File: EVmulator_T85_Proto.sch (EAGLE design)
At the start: 24 parts, among them Q2 DMN3404L-7, U1 ATTINY85V

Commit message: Finished compact version
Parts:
- added J2: (no value), Eigene-Rietig:TAG-CONNECT_TC2030-MCP-NL
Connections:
- new net !RESET: J2.5
- new net MISO: J2.1
- new net MOSI: J2.4
- new net SCK: J2.3
- new net VCC: J2.2
- net GND: now also J2.6
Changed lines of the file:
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@@
 <part name="R10" library="rcl" library_urn="urn:adsk.eagle:library:334" deviceset="R-EU_" device="R0603" package3d_urn="urn:adsk.eagle:package:23555/3" value="1k"/>
 <part name="Q2" library="SparkFun-DiscreteSemi" library_urn="urn:adsk.eagle:library:514" deviceset="MOSFET-NCH" device="-AO3404A" package3d_urn="urn:adsk.eagle:package:38446/1" value="DMN3404L-7"/>
+<part name="J2" library="Eigene-Rietig" library_urn="urn:adsk.eagle:library:40964436" deviceset="TAG-CONNECT_TC2030" device="-MCP-NL" package3d_urn="urn:adsk.eagle:package:41146494/1"/>
+<part name="GND12" library="supply1" library_urn="urn:adsk.eagle:library:371" deviceset="GND" device=""/>
 </parts>
 <sheets>
@@
 <text x="220.98" y="55.88" size="1.778" layer="91">6pin TagConnect
 Pinout 6pin ISP compatible</text>
+<text x="195.58" y="50.8" size="1.27" layer="91">ISP</text>
+<text x="170.18" y="55.88" size="1.778" layer="91">6pin TagConnect
+Pinout 6pin ISP compatible</text>
 </plain>
 <instances>
@@
 <attribute name="NAME" x="198.12" y="129.54" size="1.778" layer="96" rot="R180"/>
 <attribute name="VALUE" x="198.12" y="106.68" size="1.778" layer="96" rot="R90"/>
+</instance>
+<instance part="J2" gate="G$1" x="190.5" y="53.34" smashed="yes"/>
+<instance part="GND12" gate="1" x="185.42" y="33.02" smashed="yes">
+<attribute name="VALUE" x="182.88" y="30.48" size="1.778" layer="96"/>
 </instance>
 </instances>
@@
 <pinref part="R9" gate="G$1" pin="1"/>
 <wire x1="177.8" y1="86.36" x2="177.8" y2="88.9" width="0.1524" layer="91"/>
+</segment>
+<segment>
+<pinref part="J2" gate="G$1" pin="6"/>
+<pinref part="GND12" gate="1" pin="GND"/>
+<wire x1="187.96" y1="38.1" x2="185.42" y2="38.1" width="0.1524" layer="91"/>
+<wire x1="185.42" y1="38.1" x2="185.42" y2="35.56" width="0.1524" layer="91"/>
 </segment>
 </net>
@@
 </segment>
 </net>
+<net name="MOSI" class="0">
+<segment>
+<wire x1="182.88" y1="43.18" x2="187.96" y2="43.18" width="0.1524" layer="91"/>
+<pinref part="J2" gate="G$1" pin="4"/>
+<label x="182.88" y="43.18" size="1.27" layer="95" rot="R180" xref="yes"/>
+</segment>
+</net>
+<net name="!RESET" class="0">
+<segment>
+<wire x1="182.88" y1="40.64" x2="187.96" y2="40.64" width="0.1524" layer="91"/>
+<pinref part="J2" gate="G$1" pin="5"/>
+<label x="182.88" y="40.64" size="1.27" layer="95" rot="R180" xref="yes"/>
+</segment>
+</net>
+<net name="SCK" class="0">
+<segment>
+<wire x1="182.88" y1="45.72" x2="187.96" y2="45.72" width="0.1524" layer="91"/>
+<pinref part="J2" gate="G$1" pin="3"/>
+<label x="182.88" y="45.72" size="1.27" layer="95" rot="R180" xref="yes"/>
+</segment>
+</net>
+<net name="VCC" class="0">
+<segment>
+<wire x1="182.88" y1="48.26" x2="187.96" y2="48.26" width="0.1524" layer="91"/>
+<pinref part="J2" gate="G$1" pin="2"/>
+<label x="182.88" y="48.26" size="1.27" layer="95" rot="R180" xref="yes"/>
+</segment>
+</net>
+<net name="MISO" class="0">
+<segment>
+<wire x1="182.88" y1="50.8" x2="187.96" y2="50.8" width="0.1524" layer="91"/>
+<pinref part="J2" gate="G$1" pin="1"/>
+<label x="182.88" y="50.8" size="1.27" layer="95" rot="R180" xref="yes"/>
+</segment>
+</net>

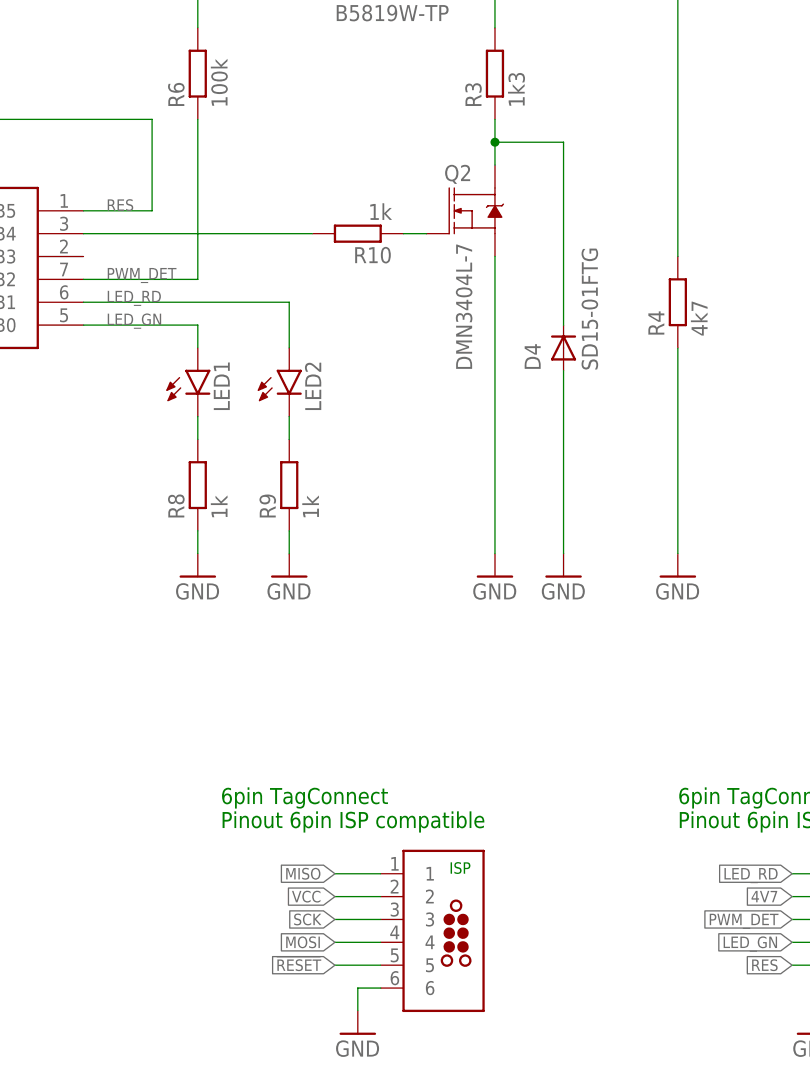
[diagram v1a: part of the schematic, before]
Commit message: changed silkscreen for the 3pin header on both boards. Updated gerbers.
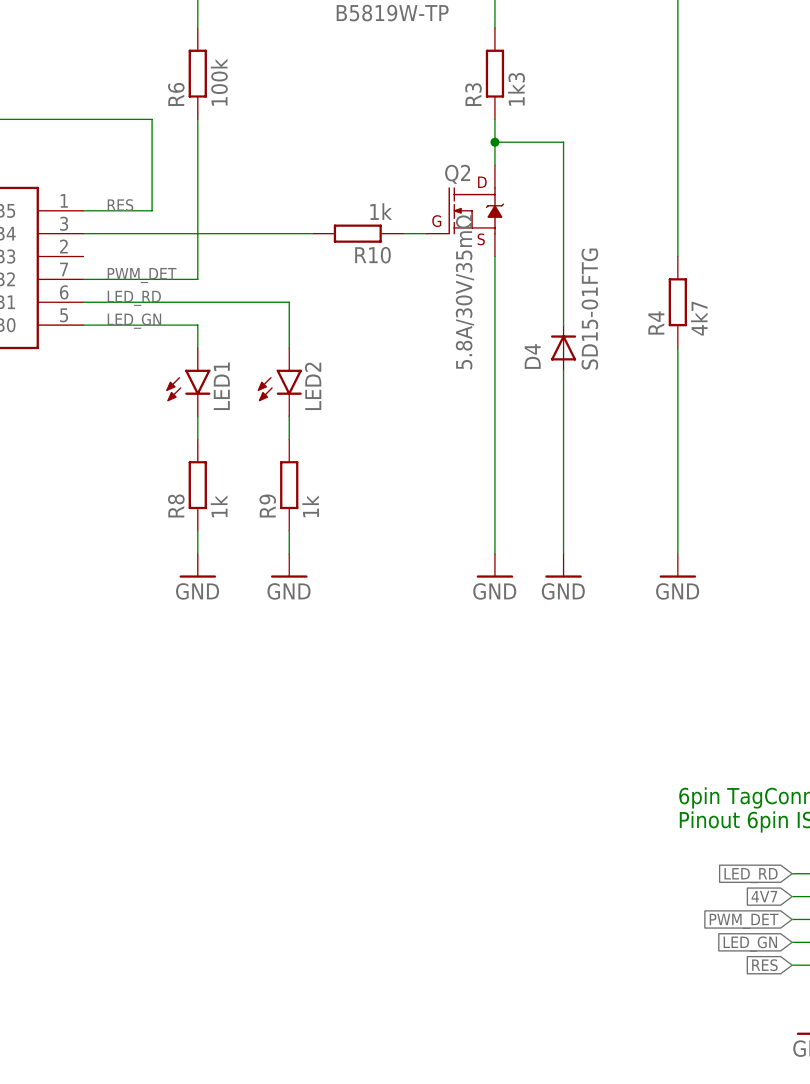
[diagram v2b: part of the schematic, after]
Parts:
- removed J2: (no value), Eigene-Rietig:TAG-CONNECT_TC2030-MCP-NL
- Q2: value DMN3404L-7 -> 5.8A/30V/35mΩ
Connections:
- removed net !RESET: J2.5
- removed net MISO: J2.1
- removed net MOSI: J2.4
- removed net SCK: J2.3
- removed net VCC: J2.2
- net GND: no longer J2.6
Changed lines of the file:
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@@
 <layer number="156" name="DXF0409-TOP" color="7" fill="1" visible="no" active="no"/>
 <layer number="157" name="DXF0409-BOTTOM" color="7" fill="1" visible="no" active="no"/>
+<layer number="158" name="FaceMMeas" color="3" fill="1" visible="no" active="no"/>
+<layer number="159" name="Geh-Bear2" color="1" fill="7" visible="no" active="no"/>
+<layer number="160" name="Topologie" color="9" fill="1" visible="no" active="no"/>
+<layer number="161" name="tomplace2" color="7" fill="1" visible="no" active="no"/>
 <layer number="166" name="AntennaArea" color="7" fill="1" visible="yes" active="yes"/>
 <layer number="168" name="4mmHeightArea" color="7" fill="1" visible="yes" active="yes"/>
@@
 <layer number="250" name="Descript" color="3" fill="1" visible="no" active="no"/>
 <layer number="251" name="SMDround" color="12" fill="11" visible="no" active="no"/>
+<layer number="252" name="BR-BS" color="7" fill="1" visible="no" active="no"/>
+<layer number="253" name="Extra" color="7" fill="1" visible="no" active="no"/>
 <layer number="254" name="cooling" color="7" fill="1" visible="yes" active="yes"/>
 <layer number="255" name="routoute" color="7" fill="1" visible="yes" active="yes"/>
@@
 <part name="GND2" library="supply1" library_urn="urn:adsk.eagle:library:371" deviceset="GND" device=""/>
 <part name="J1" library="Eigene-Rietig" library_urn="urn:adsk.eagle:library:40964436" deviceset="TAG-CONNECT_TC2030" device="-MCP-NL" package3d_urn="urn:adsk.eagle:package:41146494/1"/>
-<part name="U1" library="Eigene-Rietig" library_urn="urn:adsk.eagle:library:40964436" deviceset="ATTINY25/45/85" device="-20SU" package3d_urn="urn:adsk.eagle:package:41055619/2" value="ATTINY85V"/>
-<part name="SV1" library="con-lstb" library_urn="urn:adsk.eagle:library:162" deviceset="MA03-1" device="" package3d_urn="urn:adsk.eagle:package:8339/1"/>
+<part name="U1" library="Eigene-Rietig" library_urn="urn:adsk.eagle:library:40964436" deviceset="ATTINY25/45/85" device="-20SU" package3d_urn="urn:adsk.eagle:package:41055619/3" value="ATTINY85V"/>
+<part name="SV1" library="con-lstb" library_urn="urn:adsk.eagle:library:41989194" deviceset="MA03-1" device="" package3d_urn="urn:adsk.eagle:package:43315831/1"/>
 <part name="GND3" library="supply1" library_urn="urn:adsk.eagle:library:371" deviceset="GND" device=""/>
 <part name="GND4" library="supply1" library_urn="urn:adsk.eagle:library:371" deviceset="GND" device=""/>
@@
 <part name="GND11" library="supply1" library_urn="urn:adsk.eagle:library:371" deviceset="GND" device=""/>
 <part name="R10" library="rcl" library_urn="urn:adsk.eagle:library:334" deviceset="R-EU_" device="R0603" package3d_urn="urn:adsk.eagle:package:23555/3" value="1k"/>
-<part name="Q2" library="SparkFun-DiscreteSemi" library_urn="urn:adsk.eagle:library:514" deviceset="MOSFET-NCH" device="-AO3404A" package3d_urn="urn:adsk.eagle:package:38446/1" value="DMN3404L-7"/>
-<part name="J2" library="Eigene-Rietig" library_urn="urn:adsk.eagle:library:40964436" deviceset="TAG-CONNECT_TC2030" device="-MCP-NL" package3d_urn="urn:adsk.eagle:package:41146494/1"/>
-<part name="GND12" library="supply1" library_urn="urn:adsk.eagle:library:371" deviceset="GND" device=""/>
+<part name="Q2" library="SparkFun-DiscreteSemi" library_urn="urn:adsk.eagle:library:514" deviceset="MOSFET-NCH" device="-AO3404A" package3d_urn="urn:adsk.eagle:package:38446/2" value="5.8A/30V/35mΩ"/>
 </parts>
 <sheets>
@@
 <text x="220.98" y="55.88" size="1.778" layer="91">6pin TagConnect
 Pinout 6pin ISP compatible</text>
-<text x="195.58" y="50.8" size="1.27" layer="91">ISP</text>
-<text x="170.18" y="55.88" size="1.778" layer="91">6pin TagConnect
-Pinout 6pin ISP compatible</text>
 </plain>
 <instances>
@@
 <attribute name="NAME" x="198.12" y="129.54" size="1.778" layer="96" rot="R180"/>
 <attribute name="VALUE" x="198.12" y="106.68" size="1.778" layer="96" rot="R90"/>
-</instance>
-<instance part="J2" gate="G$1" x="190.5" y="53.34" smashed="yes"/>
-<instance part="GND12" gate="1" x="185.42" y="33.02" smashed="yes">
-<attribute name="VALUE" x="182.88" y="30.48" size="1.778" layer="96"/>
 </instance>
 </instances>
@@
 <pinref part="R9" gate="G$1" pin="1"/>
 <wire x1="177.8" y1="86.36" x2="177.8" y2="88.9" width="0.1524" layer="91"/>
-</segment>
-<segment>
-<pinref part="J2" gate="G$1" pin="6"/>
-<pinref part="GND12" gate="1" pin="GND"/>
-<wire x1="187.96" y1="38.1" x2="185.42" y2="38.1" width="0.1524" layer="91"/>
-<wire x1="185.42" y1="38.1" x2="185.42" y2="35.56" width="0.1524" layer="91"/>
 </segment>
 </net>
@@
 </segment>
 </net>
-<net name="MOSI" class="0">
-<segment>
-<wire x1="182.88" y1="43.18" x2="187.96" y2="43.18" width="0.1524" layer="91"/>
-<pinref part="J2" gate="G$1" pin="4"/>
-<label x="182.88" y="43.18" size="1.27" layer="95" rot="R180" xref="yes"/>
-</segment>
-</net>
-<net name="!RESET" class="0">
-<segment>
-<wire x1="182.88" y1="40.64" x2="187.96" y2="40.64" width="0.1524" layer="91"/>
-<pinref part="J2" gate="G$1" pin="5"/>
-<label x="182.88" y="40.64" size="1.27" layer="95" rot="R180" xref="yes"/>
-</segment>
-</net>
-<net name="SCK" class="0">
-<segment>
-<wire x1="182.88" y1="45.72" x2="187.96" y2="45.72" width="0.1524" layer="91"/>
-<pinref part="J2" gate="G$1" pin="3"/>
-<label x="182.88" y="45.72" size="1.27" layer="95" rot="R180" xref="yes"/>
-</segment>
-</net>
-<net name="VCC" class="0">
-<segment>
-<wire x1="182.88" y1="48.26" x2="187.96" y2="48.26" width="0.1524" layer="91"/>
-<pinref part="J2" gate="G$1" pin="2"/>
-<label x="182.88" y="48.26" size="1.27" layer="95" rot="R180" xref="yes"/>
-</segment>
-</net>
-<net name="MISO" class="0">
-<segment>
-<wire x1="182.88" y1="50.8" x2="187.96" y2="50.8" width="0.1524" layer="91"/>
-<pinref part="J2" gate="G$1" pin="1"/>
-<label x="182.88" y="50.8" size="1.27" layer="95" rot="R180" xref="yes"/>
-</segment>
-</net>
